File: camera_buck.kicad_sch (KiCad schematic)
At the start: 21 parts, among them IC1 SiC437BED-T1-GE3, J601 Conn_01x02_Male

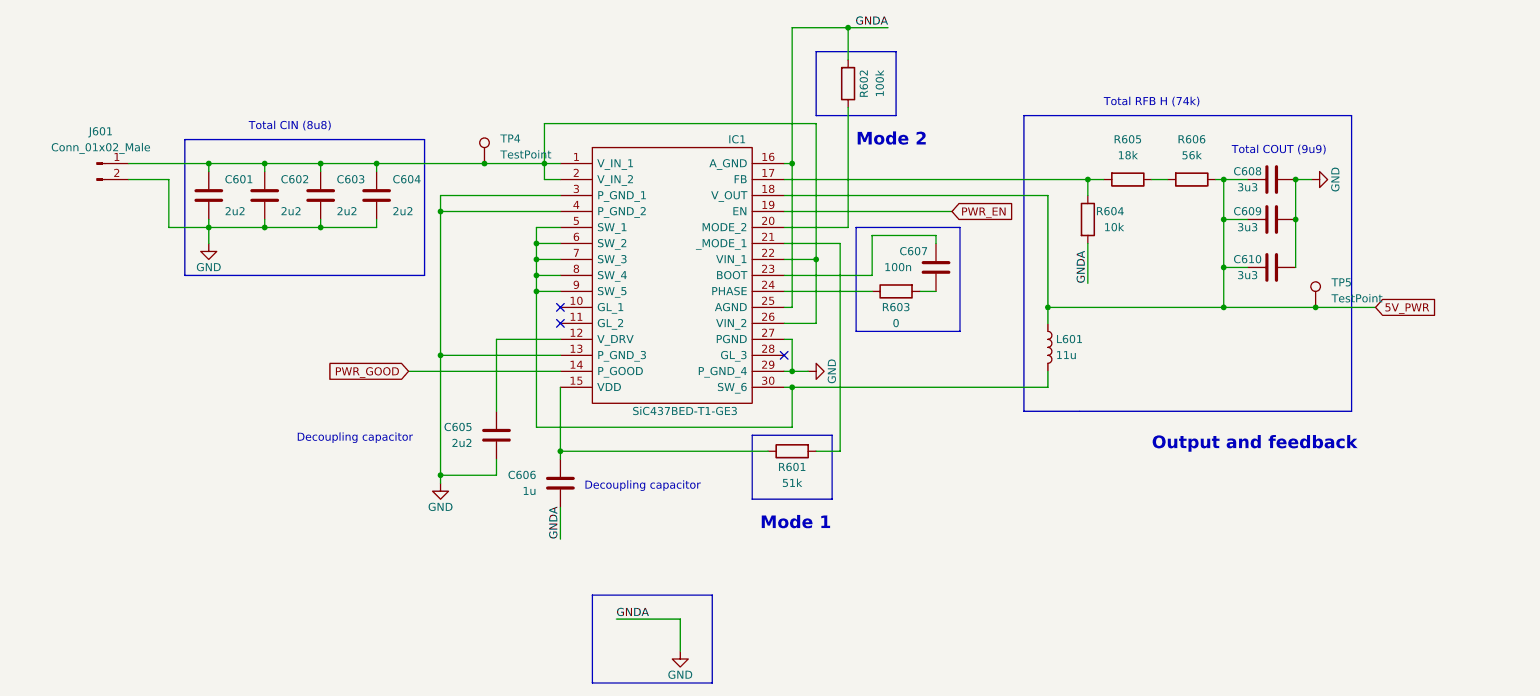
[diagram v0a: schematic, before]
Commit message: File names and ERC
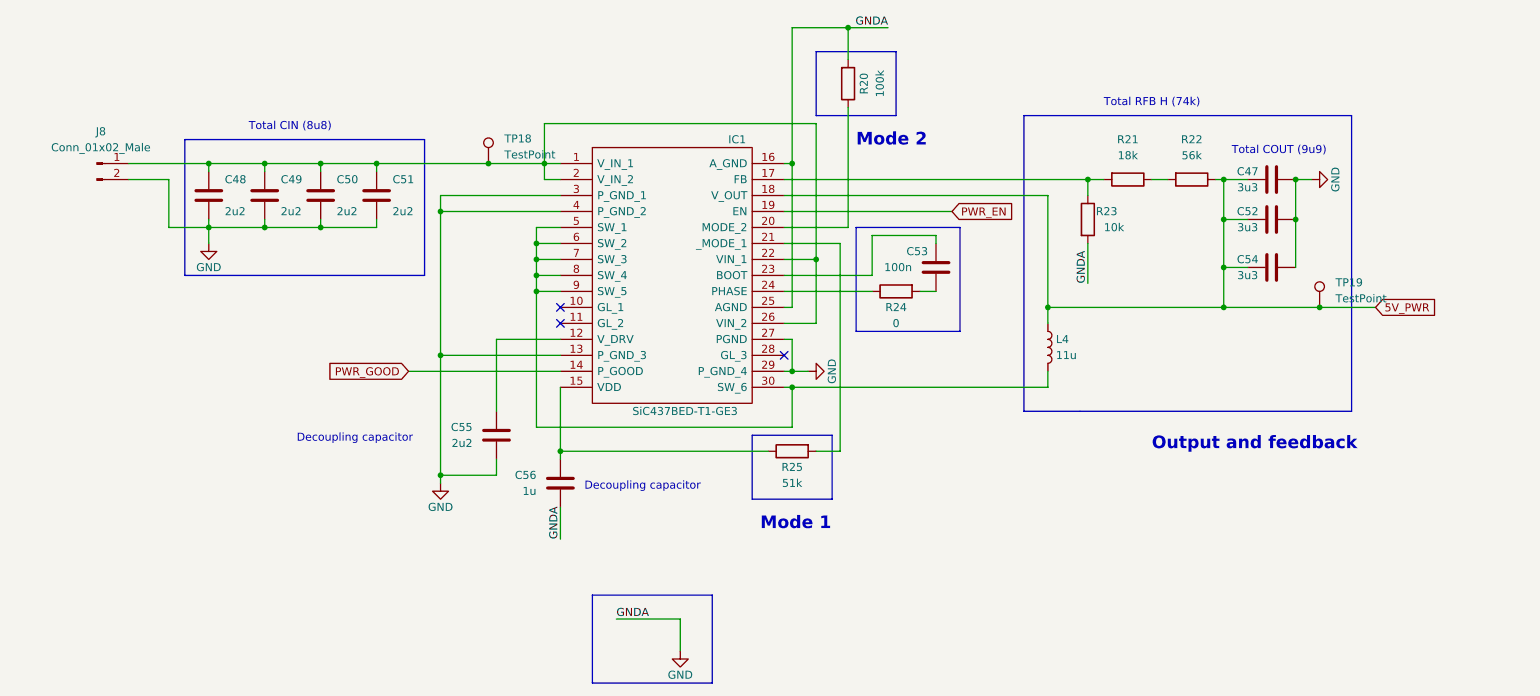
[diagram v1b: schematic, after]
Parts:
- renumbered C608 to C47, C601 to C48, C602 to C49, C603 to C50, C604 to C51, C609 to C52, C607 to C53, C610 to C54, C605 to C55, C606 to C56, J601 to J8, L601 to L4, R602 to R20, R605 to R21, R606 to R22, R604 to R23, R603 to R24, R601 to R25, TP4 to TP18, TP5 to TP19
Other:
- moved on the sheet: TP18, TP19

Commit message: Fixed libraries and footprints
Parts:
- IC1: footprint SIC437BED-T1-GE3:SIC437BEDT1GE3 -> fps:SiC437BEDT1GE3
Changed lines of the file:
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@@
       (effects (font (size 1.27 1.27)) (justify left))
     )
-    (property "Footprint" "SIC437BED-T1-GE3:SIC437BEDT1GE3" (at 158.75 74.93 0)
+    (property "Footprint" "fps:SiC437BEDT1GE3" (at 158.75 74.93 0)
       (effects (font (size 1.27 1.27)) (justify left) hide)
     )

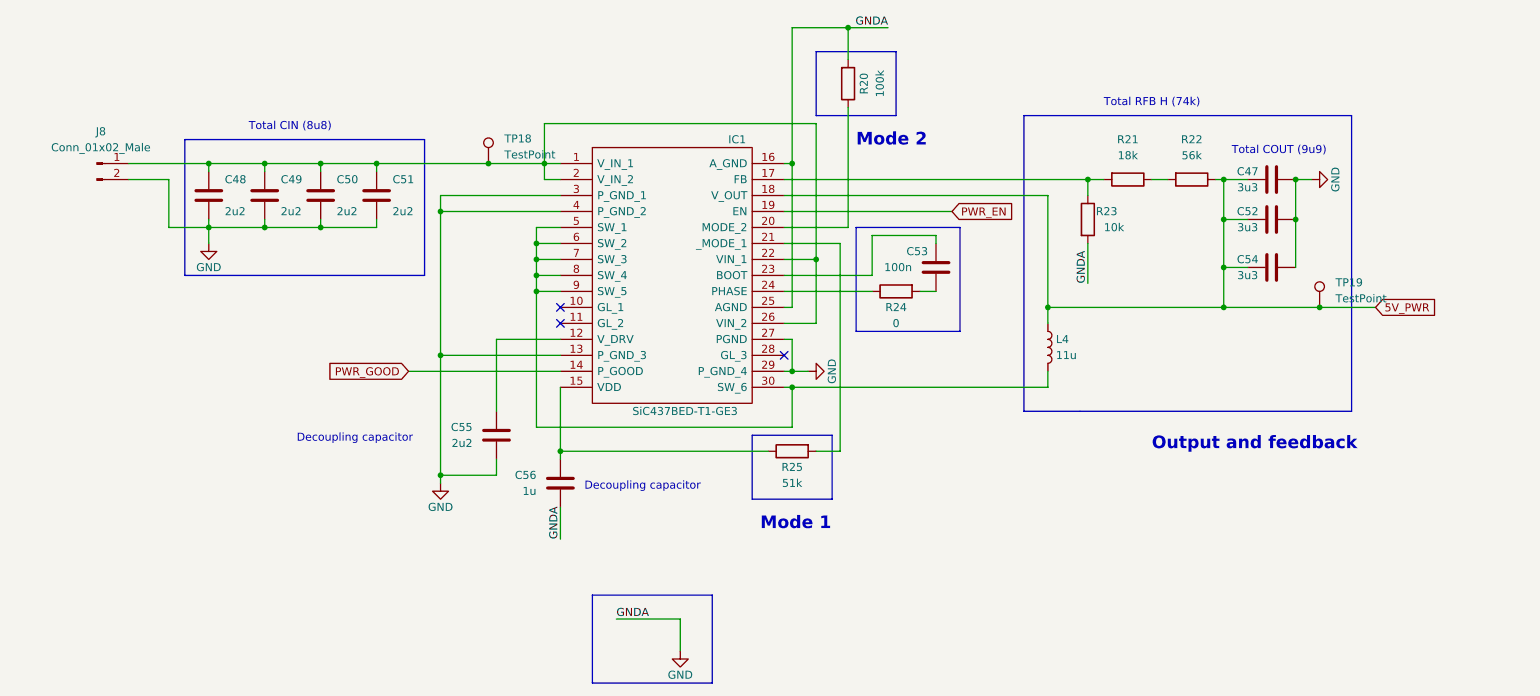
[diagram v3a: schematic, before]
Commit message: Camera buck changes, c and r footprints, other
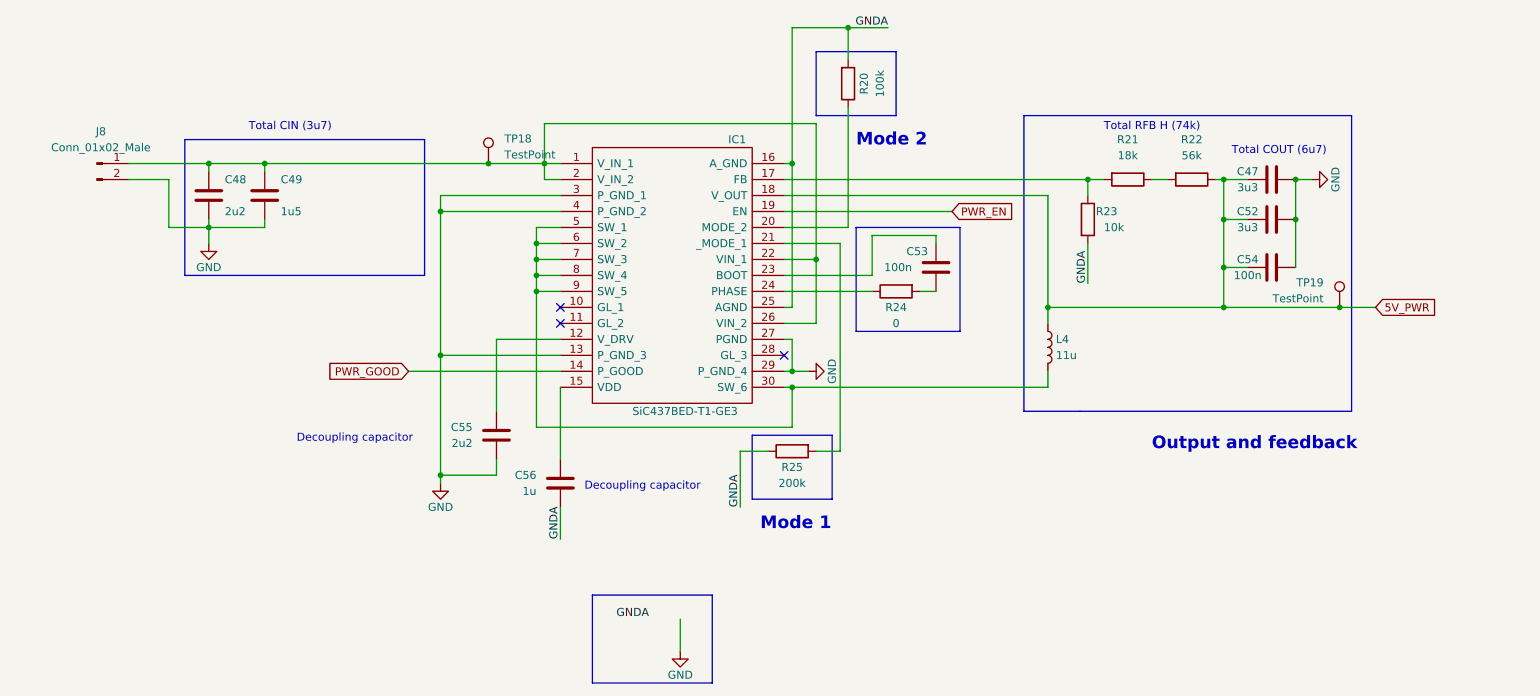
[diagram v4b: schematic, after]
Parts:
- removed C50, C51: 2u2, Capacitor_SMD:C_0603_1608Metric, symbol Device:C
- C49: value 2u2 -> 1u5
- C54: value 3u3 -> 100n; footprint Capacitor_SMD:C_0603_1608Metric -> Capacitor_SMD:C_0402_1005Metric
- C55, C56: footprint Capacitor_SMD:C_0603_1608Metric -> Capacitor_SMD:C_0402_1005Metric
- L4: footprint Inductor_SMD:L_0805_2012Metric -> Ricardo-CHEESE:IND_ASPI-0630HI-6R8M-T15
- R25: value 51k -> 200k
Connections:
- net GND: no longer C56.1, IC1.16 (A_GND), IC1.25 (AGND), R20.2, R23.2
- net at C56.2, IC1.15 (VDD): no longer R25.1
- new net GNDA: C56.1, IC1.16 (A_GND), IC1.25 (AGND), R20.2, R23.2, R25.1
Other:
- note added: "Total CIN (3u7)"
- note added: "Total COUT (6u7)"
- note removed: "Total CIN (8u8)"
- note removed: "Total COUT (9u9)"
- moved on the sheet: TP19

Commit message: radio side needs reviewing
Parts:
- removed C47: 3u3, Capacitor_SMD:C_0603_1608Metric, symbol Device:C
- C48: value 2u2 -> 10uF
- C49: value 1u5 -> 100nF; footprint Capacitor_SMD:C_0603_1608Metric -> Capacitor_SMD:C_0402_1005Metric
- C52: value 3u3 -> 47uF; footprint Capacitor_SMD:C_0603_1608Metric -> Capacitor_SMD:C_1206_3216Metric
- IC1: footprint fps:SiC437BEDT1GE3 -> iclr:SiC437BEDT1GE3
- J8: footprint Connector:JWT_A3963_1x02_P3.96mm_Vertical -> Connector_AMASS:AMASS_XT30PW-M_1x02_P2.50mm_Horizontal
- L4: value 11u -> 3.3uH; footprint Ricardo-CHEESE:IND_ASPI-0630HI-6R8M-T15 -> iclr:INDPM110100X540N
- R20: value 100k -> 51k
- R25: value 200k -> 100k
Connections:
- net GNDA is gone; now on net GND: C56.1, IC1.16 (A_GND), IC1.25 (AGND), R20.2, R23.2, R25.1
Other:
- note removed: "Total CIN (3u7)"
- note removed: "Total COUT (6u7)"
- moved on the sheet: C52, C54

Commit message: post andrei review
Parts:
- removed TP18, TP19: TestPoint, TestPoint:TestPoint_Pad_D1.0mm, symbol Connector:TestPoint
- added R26: 51k, Resistor_SMD:R_0402_1005Metric, symbol Device:R
- C48: value 10uF -> 47uF; footprint Capacitor_SMD:C_0603_1608Metric -> Capacitor_SMD:C_1206_3216Metric
- R24: value 0 -> 2.2; footprint Resistor_SMD:R_0603_1608Metric -> Resistor_SMD:R_0402_1005Metric
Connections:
- net GND: now also J8.1 (Pin_1); no longer J8.2 (Pin_2)
- net at C48.1, C49.1, IC1.1 (V_IN_1)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: now also J8.2 (Pin_2); no longer J8.1 (Pin_1)
- net at C56.2, IC1.15 (VDD): now also R26.1
- net PWR_GOOD: no longer names the net of IC1.14 (P_GOOD)
- net PWR_GOOD: now also R26.2
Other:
- moved on the sheet: J8

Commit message: fixed some stuff
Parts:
- added R3: 10k, Resistor_SMD:R_0402_1005Metric, symbol Device:R_Small
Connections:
- net GND: now also R3.2
- net PWR_EN: now also R3.1
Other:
- moved on the sheet: C52, C54, L4, R21, R22, R23
